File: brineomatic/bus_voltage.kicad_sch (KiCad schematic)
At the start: 5 parts

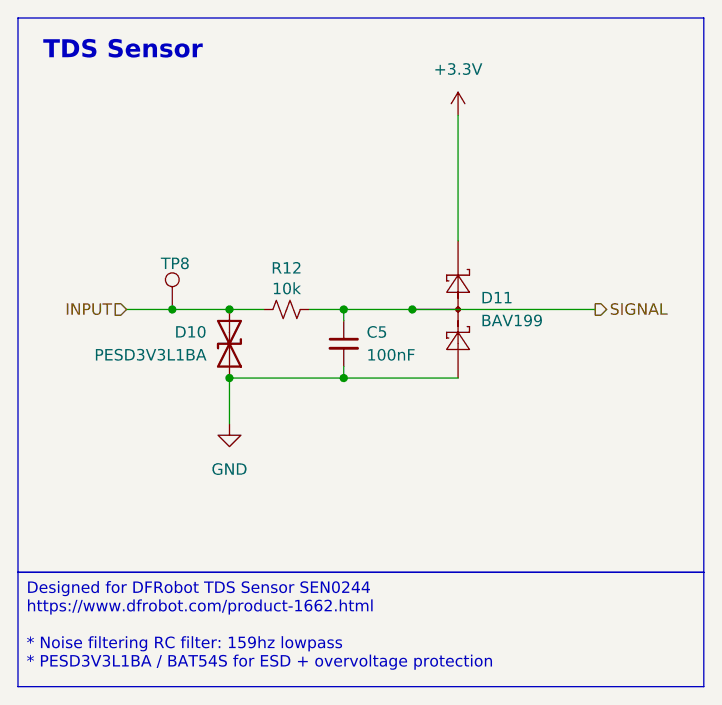
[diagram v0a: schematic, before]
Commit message: Updating schematic for Rev D: * Original ADS1115   * brine tds (same)   * product tds (same)   * bus voltage (new)   * spare 4-20ma sensor (new)
* Add 2nd ADS1115 -> only 4-20ma sensors
  * pre-filter pressure - jst 2.0
  * mid-filter pressure - jst 2.0
  * post-filter pressure - jst 2.0
  * high pressure - jst 2.0
  * alert pin -> gpio3
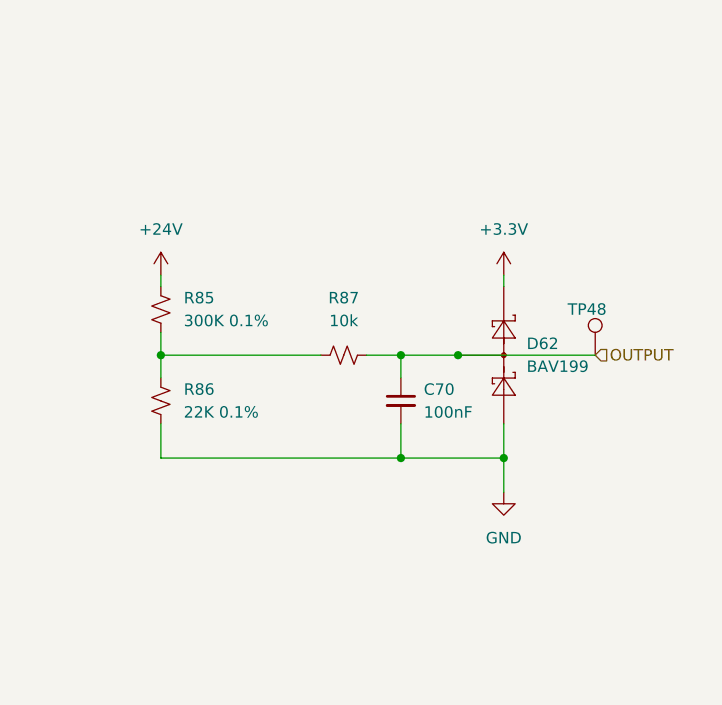
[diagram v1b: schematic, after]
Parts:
- removed C5: 100nF, Capacitor_SMD:C_0603_1608Metric, symbol Device:C_Small
- removed D10: PESD3V3L1BA, Diode_SMD:D_SOD-323, symbol Device:D_TVS
- removed D11: BAV199, Package_TO_SOT_SMD:SOT-23, symbol Diode:BAT54S
- removed R12: 10k, Resistor_SMD:R_0603_1608Metric, symbol Device:R_Small_US
- removed TP8: TestPoint, TestPoint:TestPoint_Pad_D1.5mm, symbol Connector:TestPoint
- added C70: 100nF, Capacitor_SMD:C_0603_1608Metric, symbol Device:C_Small
- added D62: BAV199, Package_TO_SOT_SMD:SOT-23, symbol Diode:BAT54S
- added R85: 300K 0.1%, Resistor_SMD:R_0603_1608Metric, symbol Device:R_Small_US
- added R86: 22K 0.1%, Resistor_SMD:R_0603_1608Metric, symbol Device:R_Small_US
- added R87: 10k, Resistor_SMD:R_0603_1608Metric, symbol Device:R_Small_US
- added TP48: TestPoint, TestPoint:TestPoint_Pad_D1.5mm, symbol yarrboard:TestPoint
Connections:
- net +3.3V: now also D62.2 (K)
- net GND: now also C70.2, D62.1 (A), R86.1
- new net: R85.1, R86.2, R87.1
- new net +24V: R85.2
- new net OUTPUT: C70.1, D62.3 (COM), R87.2, TP48.1
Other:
- note removed: "TDS Sensor"

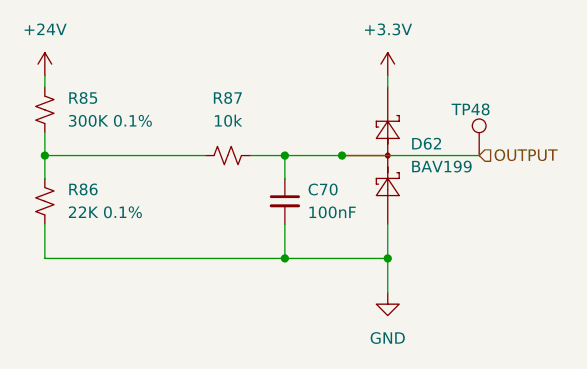
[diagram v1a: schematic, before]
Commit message: tds sensor input -> pin header 2.54 3x03
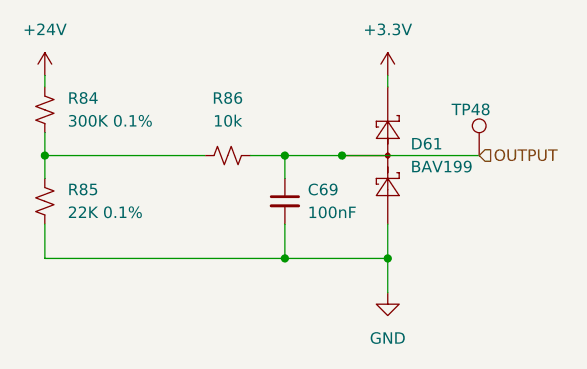
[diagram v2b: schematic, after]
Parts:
- renumbered C70 to C69, D62 to D61, R85 to R84, R86 to R85, R87 to R86
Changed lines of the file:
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@@
 		(dnp no)
 		(fields_autoplaced yes)
-		(property "Reference" "D62"
+		(property "Reference" "D61"
 			(at 138.43 88.9 90)
 			(effects
@@
 			(project "brineomatic"
 				(path "/96477ae2-ef08-48f3-8dd4-fe4478541f68/7bf78c34-2cd5-4c8a-93cc-e0889dc1ff3c"
-					(reference "D62")
+					(reference "D61")
 					(unit 1)
 				)
@@
 		(dnp no)
 		(fields_autoplaced yes)
-		(property "Reference" "#PWR091"
+		(property "Reference" "#PWR089"
 			(at 135.89 111.76 0)
 			(effects
@@
 			(project "brineomatic"
 				(path "/96477ae2-ef08-48f3-8dd4-fe4478541f68/7bf78c34-2cd5-4c8a-93cc-e0889dc1ff3c"
-					(reference "#PWR091")
+					(reference "#PWR089")
 					(unit 1)
 				)
@@
 		(dnp no)
 		(fields_autoplaced yes)
-		(property "Reference" "#PWR090"
+		(property "Reference" "#PWR088"
 			(at 135.89 85.09 0)
 			(effects
@@
 			(project "brineomatic"
 				(path "/96477ae2-ef08-48f3-8dd4-fe4478541f68/7bf78c34-2cd5-4c8a-93cc-e0889dc1ff3c"
-					(reference "#PWR090")
+					(reference "#PWR088")
 					(unit 1)
 				)
@@
 		(dnp no)
 		(fields_autoplaced yes)
-		(property "Reference" "R85"
+		(property "Reference" "R84"
 			(at 100.33 83.82 0)
 			(effects
@@
 			(project "brineomatic"
 				(path "/96477ae2-ef08-48f3-8dd4-fe4478541f68/7bf78c34-2cd5-4c8a-93cc-e0889dc1ff3c"
-					(reference "R85")
+					(reference "R84")
 					(unit 1)
 				)
@@
 		(dnp no)
 		(fields_autoplaced yes)
-		(property "Reference" "R87"
+		(property "Reference" "R86"
 			(at 118.11 83.82 90)
 			(effects
@@
 			(project "brineomatic"
 				(path "/96477ae2-ef08-48f3-8dd4-fe4478541f68/7bf78c34-2cd5-4c8a-93cc-e0889dc1ff3c"
-					(reference "R87")
+					(reference "R86")
 					(unit 1)
 				)
@@
 		(dnp no)
 		(fields_autoplaced yes)
-		(property "Reference" "#PWR089"
+		(property "Reference" "#PWR087"
 			(at 97.79 85.09 0)
 			(effects
@@
 			(project "brineomatic"
 				(path "/96477ae2-ef08-48f3-8dd4-fe4478541f68/7bf78c34-2cd5-4c8a-93cc-e0889dc1ff3c"
-					(reference "#PWR089")
+					(reference "#PWR087")
 					(unit 1)
 				)
@@
 		(on_board yes)
 		(dnp no)
-		(property "Reference" "C70"
+		(property "Reference" "C69"
 			(at 127 93.9863 0)
 			(effects
@@
 			(project "brineomatic"
 				(path "/96477ae2-ef08-48f3-8dd4-fe4478541f68/7bf78c34-2cd5-4c8a-93cc-e0889dc1ff3c"
-					(reference "C70")
+					(reference "C69")
 					(unit 1)
 				)
@@
 		(dnp no)
 		(fields_autoplaced yes)
-		(property "Reference" "R86"
+		(property "Reference" "R85"
 			(at 100.33 93.98 0)
 			(effects
@@
 			(project "brineomatic"
 				(path "/96477ae2-ef08-48f3-8dd4-fe4478541f68/7bf78c34-2cd5-4c8a-93cc-e0889dc1ff3c"
-					(reference "R86")
-					(unit 1)
-				)
+					(reference "R85")
+					(unit 1)
+				)
